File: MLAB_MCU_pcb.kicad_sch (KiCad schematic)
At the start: 100 parts, among them J1 Conn_01x02_Pin, J10 Conn_01x02_Pin, J11 Conn_01x02_Pin, J12 Conn_01x02_Pin, J13 Conn_01x02_Pin, J14 Conn_01x02_Pin, J15 Conn_01x02_Pin, J16 Conn_01x02_Pin, J17 Conn_01x02_Pin, J18 Conn_02x05_Odd_Even, J19 Conn_02x05_Odd_Even, J2 Conn_01x02_Pin, J20 Conn_01x02_Pin, J21 Conn_01x02_Pin, J22 Conn_01x02_Pin, J23 Conn_01x02_Pin, J24 Conn_Coaxial, J25 Conn_01x02_Pin, J26 Conn_Coaxial, J27 Conn_Coaxial, J28 Conn_01x02_Pin, J29 Conn_01x02_Pin, J3 Input Header, J30 Conn_01x02_Pin, J4 TBC05-02-1-G-G, J5 232-5205-01, J6 Conn_Coaxial, J7 Conn_01x03_Pin, J8 Conn_01x02_Pin, J9 Conn_01x02_Pin, U1 TPS7A2012PDBVRG4, U2 TPS7A2033PDBVR, U3 DSC1101DL5-020.0000, U4 24LC512, U5 INA4180A1

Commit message: Initial PCB layout
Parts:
- removed C12, C13, C14: 0.1u, Capacitor_SMD:C_0805_2012Metric_Pad1.18x1.45mm_HandSolder, symbol Device:C
- removed J10, J11, J12, J13, J14, J15, J16, J17, J21, J9: Conn_01x02_Pin, Connector_PinHeader_2.54mm:PinHeader_1x02_P2.54mm_Vertical, symbol Connector:Conn_01x02_Pin
- removed R1: 1, Resistor_SMD:R_0805_2012Metric_Pad1.20x1.40mm_HandSolder, symbol Device:R
- added C18: 47u, Capacitor_THT:CP_Radial_D5.0mm_P2.00mm, symbol Device:C_Polarized
- added D11: SS34, Diode_SMD:D_SMA, symbol Diode:SS34
- added D12: SMAJ6.0A, Diode_SMD:D_SMA, symbol Diode:SMAJ6.0A
- added J31, J32: Conn_02x05_Odd_Even, Connector_PinHeader_2.54mm:PinHeader_2x05_P2.54mm_Vertical, symbol Connector_Generic:Conn_02x05_Odd_Even
- added R7: 1, Resistor_SMD:R_0805_2012Metric_Pad1.20x1.40mm_HandSolder, symbol Device:R
- C10: renamed from C18; now not fitted
- C15: renamed from C17; now not fitted
- C16: renamed from C19; now not fitted
- J10: renamed from J29; now not fitted
- J25: renamed from J28; now not fitted
- J26: renamed from J30; now not fitted
- R2: renamed from R7; now not fitted
- R33: renamed from R32; now not fitted
- R34, R8: now not fitted
- R5: renamed from R11; now not fitted
- R9: renamed from R33; now not fitted
- renumbered C7 to C11, C11 to C12, C16 to C13, C15 to C14, C3 to C2, C8 to C3, C2 to C4, C4 to C5, C5 to C6, C9 to C7, C10 to C8, C6 to C9, J4 to J1, J3 to J2, J25 to J21, J26 to J23, J27 to J24, J23 to J27, J5 to J28, J18 to J29, J6 to J3, J19 to J30, J1 to J4, J2 to J5, J20 to J6, J24 to J9, R6 to R1, R5 to R10, R12 to R11, R13 to R12, R14 to R13, R15 to R14, R16 to R15, R17 to R16, R18 to R17, R19 to R18, R20 to R19, R21 to R20, R3 to R21, R4 to R3, R2 to R32, R10 to R4, R9 to R6, U3 to U1, U1 to U2, U2 to U3
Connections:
- net +1V2: now also J8.2 (Pin_2), U5.5 (+), R7.1; no longer C8.1, C9.1, U5.3 (+)
- net +3V3: now also U5.3 (+); no longer C11.1, C12.1, U5.6 (-)
- net 0: now also J1.2 (Pin_2), J2.2 (Pin_2), C18.2, D12.2 (A2)
- net GPIO0_ISO: now also J31.1 (Pin_1); no longer J8.2 (Pin_2)
- net GPIO1_ISO: now also J31.3 (Pin_3)
- net GPIO2_ISO: now also J31.5 (Pin_5)
- net GPIO3_ISO: now also J31.7 (Pin_7)
- net GPIO4_ISO: now also J31.9 (Pin_9)
- net GPIO5_ISO: now also J32.1 (Pin_1)
- net GPIO6_ISO: now also J32.3 (Pin_3)
- net GPIO7_ISO: now also J32.5 (Pin_5)
- net GPIO8_ISO: now also J32.7 (Pin_7)
- net GPIO9_ISO: now also J32.9 (Pin_9)
- net VDD_CORE: now also C8.1, C9.1, J8.1 (Pin_1), U5.6 (-), R7.2; no longer U5.2 (-)
- net VDD_IO: now also C11.1, C12.1, U5.2 (-); no longer U5.5 (+)
- net VSS: now also IC1.33 (ePad)
- net at R24.1: now also J31.6 (Pin_6)
- net at R22.1: now also J31.2 (Pin_2); no longer J8.1 (Pin_1)
- net at R25.1: now also J31.8 (Pin_8)
- net at R23.1: now also J31.4 (Pin_4)
- net at J9.1 (In), R9.1: now also U5.7; no longer U5.1
- net at J23.1 (In), R33.1: now also U5.1; no longer U5.7
- net 4-6V: now reaches C1.1, U2.1 (IN), U2.3 (EN)
- net 4-6V: now also C2.1, U3.1 (IN), U3.3 (EN), C18.1, D11.1 (K), D12.1 (A1); no longer J1.2 (Pin_2), J2.1 (Pin_1)
- net at R26.1: now also J31.10 (Pin_10)
- net at R30.1: now also J32.8 (Pin_8)
- net at R29.1: now also J32.6 (Pin_6)
- net at R28.1: now also J32.4 (Pin_4)
- net at R31.1: now also J32.10 (Pin_10)
- net at R27.1: now also J32.2 (Pin_2)
- new net: D11.2 (A), J1.1 (Pin_1), J2.1 (Pin_1)
- no-connect marks 3 -> 6
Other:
- moved on the sheet: C1, C11, C12, C2, C4, C5, C8, C9, J1, J2, J21, J22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

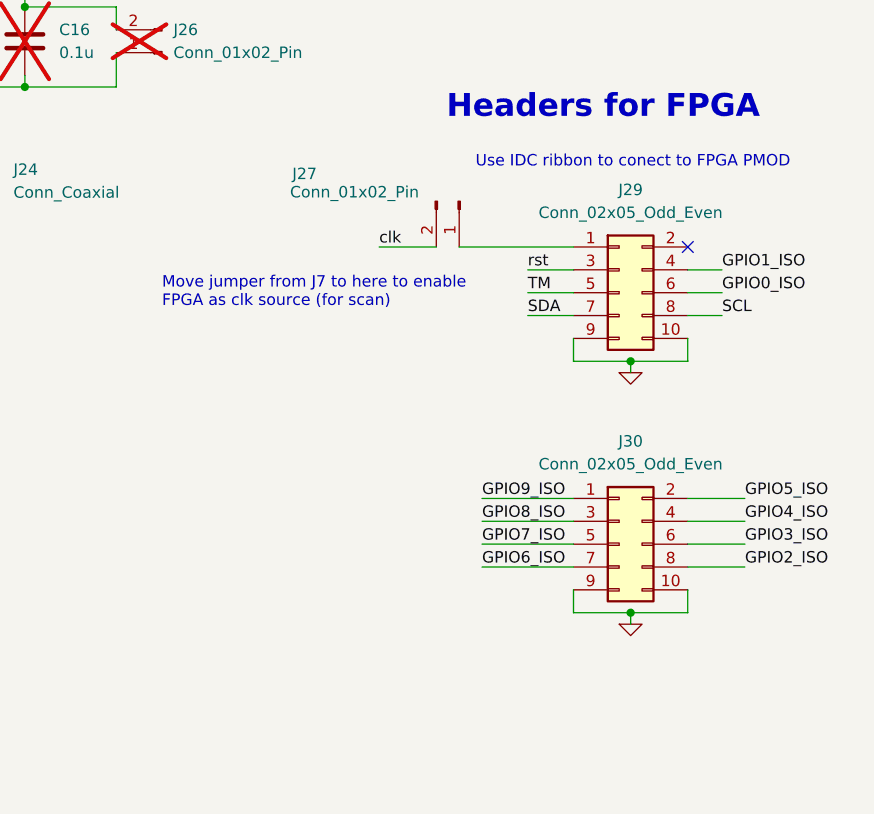
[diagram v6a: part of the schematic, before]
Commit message: Redo FPGA PMOD for direct connection; Add mounting holes in the corners
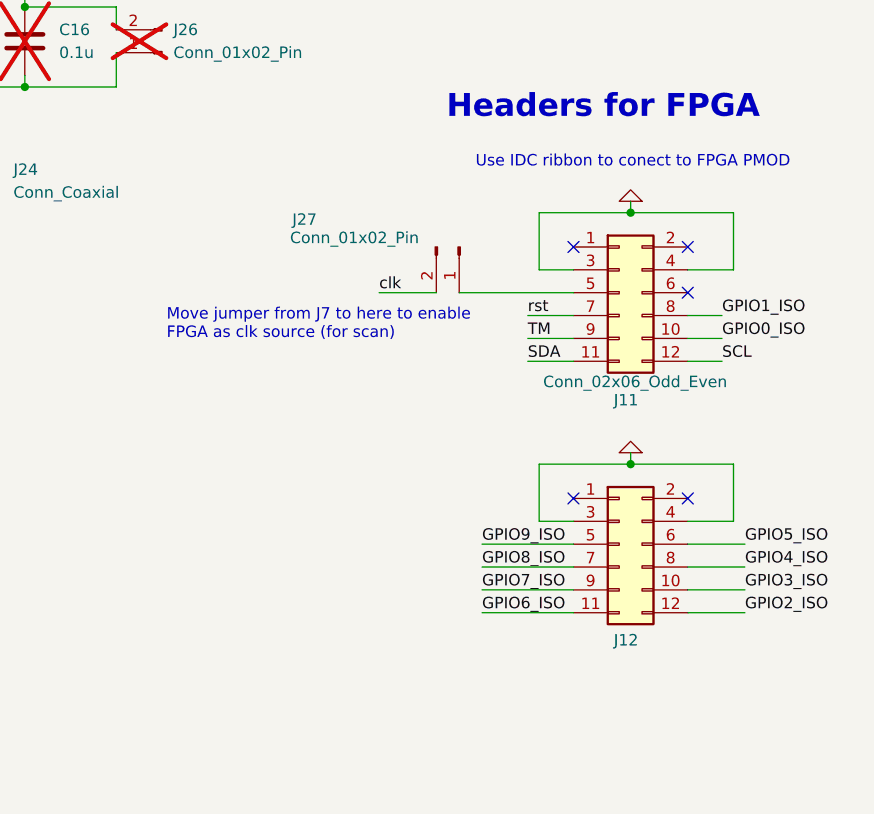
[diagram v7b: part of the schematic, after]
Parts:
- removed J29, J30: Conn_02x05_Odd_Even, Connector_PinHeader_2.54mm:PinHeader_2x05_P2.54mm_Vertical, symbol Connector_Generic:Conn_02x05_Odd_Even
- added J11, J12: Conn_02x06_Odd_Even, Connector_PinHeader_2.54mm:PinHeader_2x06_P2.54mm_Horizontal, symbol Connector_Generic:Conn_02x06_Odd_Even
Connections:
- net 0: now also J11.3 (Pin_3), J11.4 (Pin_4), J12.3 (Pin_3), J12.4 (Pin_4)
- net GPIO0_ISO: now also J11.10 (Pin_10)
- net GPIO1_ISO: now also J11.8 (Pin_8)
- net GPIO2_ISO: now also J12.12 (Pin_12)
- net GPIO3_ISO: now also J12.10 (Pin_10)
- net GPIO4_ISO: now also J12.8 (Pin_8)
- net GPIO5_ISO: now also J12.6 (Pin_6)
- net GPIO6_ISO: now also J12.11 (Pin_11)
- net GPIO7_ISO: now also J12.9 (Pin_9)
- net GPIO8_ISO: now also J12.7 (Pin_7)
- net GPIO9_ISO: now also J12.5 (Pin_5)
- net SCL: now also J11.12 (Pin_12)
- net SDA: now also J11.11 (Pin_11)
- net TM: now also J11.9 (Pin_9)
- net rst: now also J11.7 (Pin_7)
- net at J27.1 (Pin_1): now also J11.5 (Pin_5)
- no-connect marks 6 -> 10

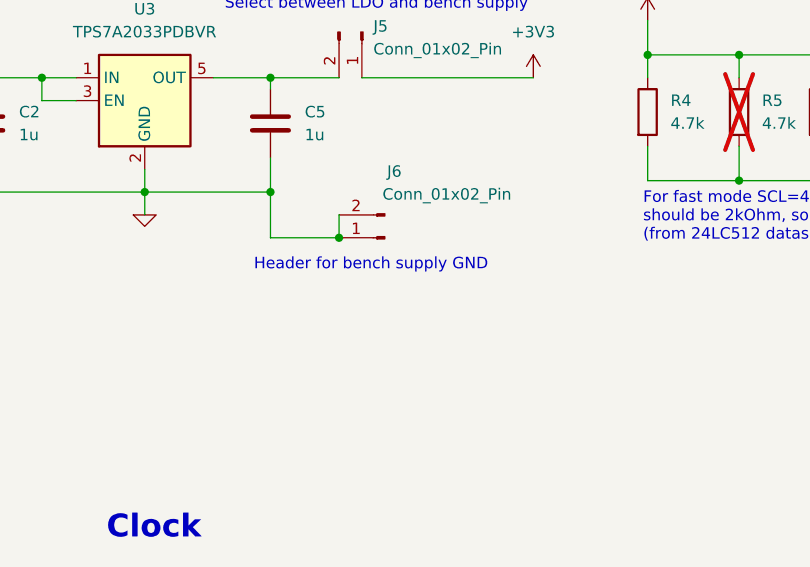
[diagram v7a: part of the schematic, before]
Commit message: Add DRC for jlcpcb; minor layout changes
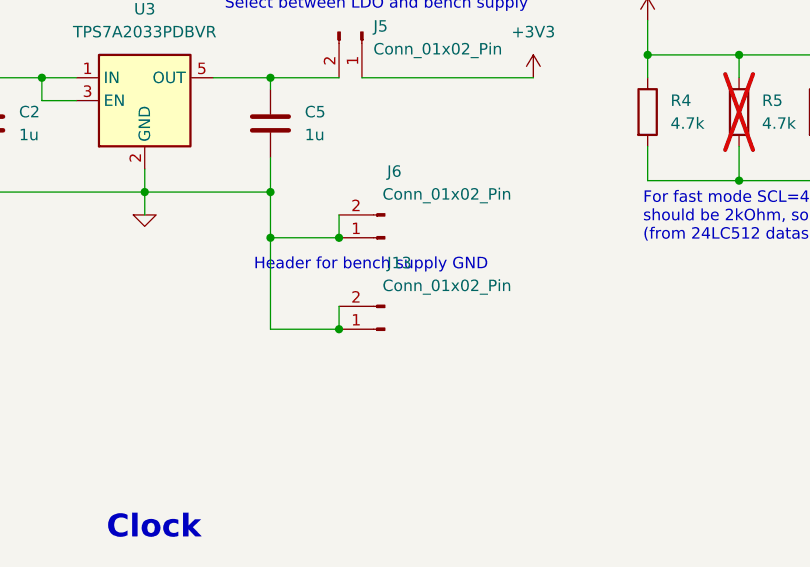
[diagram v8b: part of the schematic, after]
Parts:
- added J13: Conn_01x02_Pin, Connector_PinHeader_2.54mm:PinHeader_1x02_P2.54mm_Vertical, symbol Connector:Conn_01x02_Pin
- D11: MANUFACTURER (none) -> onsemi; MP (none) -> SS34
- D12: MANUFACTURER (none) -> Littelfuse; MP (none) -> SMAJ6.0A
- J1: MANUFACTURER (none) -> Global Connector Technology; MP (none) -> TBC05-02-1-G-G
- J23, J24, J3, J9: MANUFACTURER (none) -> Amphenol RF; MP (none) -> 132134
- J28: now left out of the parts list
- U1: MANUFACTURER (none) -> Microchip Technology; MP (none) -> DSC1101DL5-020.0000
- U2: MANUFACTURER (none) -> Texas Instruments; MP (none) -> TPS7A2012PDBVRG4
- U3: MANUFACTURER (none) -> Texas Instruments; MP (none) -> TPS7A2033PDBVR
- U4: MANUFACTURER (none) -> Microchip Technology; MP (none) -> 24LC512-I/P
- U5: MANUFACTURER (none) -> Texas Instruments; MP (none) -> INA4180A1IPWR
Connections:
- net 0: now also J13.1 (Pin_1), J13.2 (Pin_2)
